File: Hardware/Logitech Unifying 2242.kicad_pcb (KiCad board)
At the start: 2 copper layers, 22 x 42 mm, 19 parts, among them J1 Bus_M.2_Socket_B, U1 TPS613222ADBV

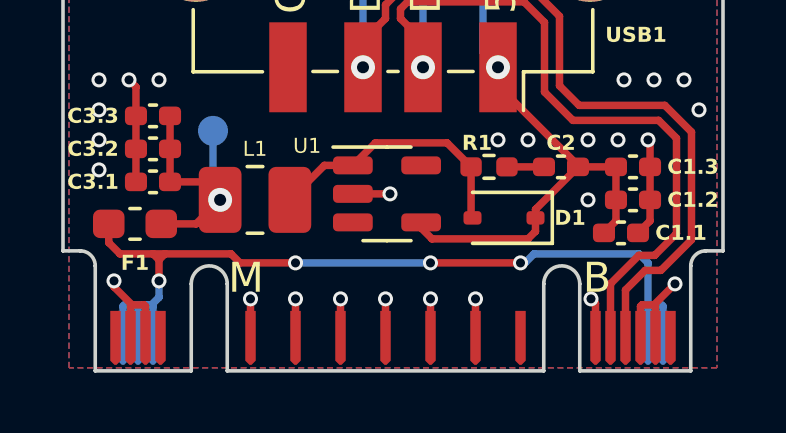
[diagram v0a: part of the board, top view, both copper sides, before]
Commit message: Adjust ground vias
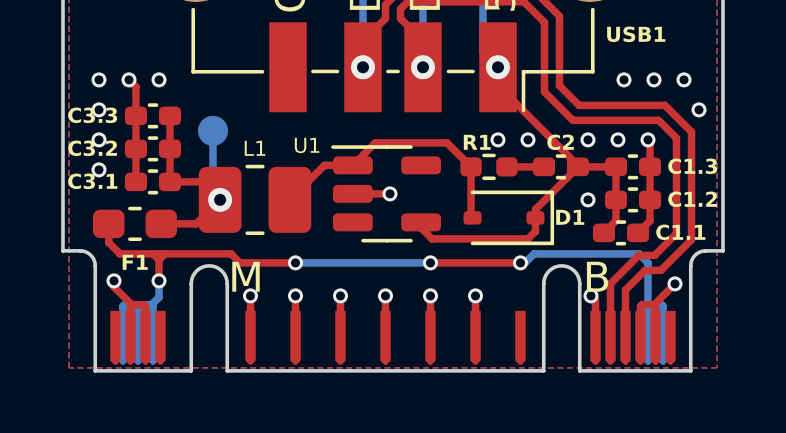
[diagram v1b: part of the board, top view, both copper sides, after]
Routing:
- net GND: track 24.5 -> 25.2 mm

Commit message: Small copper fixes
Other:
- board text added: "${TITLE} Rev.${REVISION} | ${ISSUE_DATE} ${COMMENT1}"
- board text removed: "${TITLE} Revision ${REVISION} ${COMMENT1} ${ISSUE_DATE}"
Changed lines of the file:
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@@
         (effects (font (size 1 1) (thickness 0.15)) (justify mirror))
     )
-    (fp_text user "3V3" (at 0 1.3 unlocked) (layer "B.SilkS")
+    (fp_text user "3V3" (at 0 -1.4 unlocked) (layer "B.SilkS")
         (effects (font (size 0.5 0.5) (thickness 0.1)) (justify mirror))
     )
@@
   (gr_line (start 147.1 85.2) (end 147.1 104)
     (stroke (width 0.1) (type solid)) (layer "Edge.Cuts"))
-  (gr_text "${TITLE}\nRevision ${REVISION}\n${COMMENT1}\n${ISSUE_DATE}" (at 138.6 112.8) (layer "B.SilkS")
+  (gr_text "${TITLE}\nRev.${REVISION} | ${ISSUE_DATE}\n${COMMENT1}" (at 138.6 112) (layer "B.SilkS")
     (effects (font (size 1 1) (thickness 0.2)) (justify mirror))
   )
@@
   (segment (start 132.6 113.2) (end 132.6 115.2625) (width 0.25) (layer "B.Cu") (net 14))
   (segment (start 132.6 115.2625) (end 132.8375 115.5) (width 0.25) (layer "B.Cu") (net 14))
+  (zone (net 0) (net_name "") (layer "F.Cu") (hatch edge 0.508)
+    (connect_pads (clearance 0))
+    (min_thickness 0.25) (filled_areas_thickness no)
+    (keepout (tracks allowed) (vias allowed) (pads allowed) (copperpour not_allowed) (footprints allowed))
+    (fill (thermal_gap 0.25) (thermal_bridge_width 0.25))
+    (polygon
+      (pts
+        (xy 129.7 115.3)
+        (xy 130.4 115.3)
+        (xy 130.4 116.1)
+        (xy 129.7 116.1)
+      )
+    )
+  )
   (zone (net 0) (net_name "") (layer "F.Cu") (hatch edge 0.5)
     (connect_pads (clearance 0))
@@
     (connect_pads (clearance 0.25))
     (min_thickness 0.25) (filled_areas_thickness no)
-    (fill yes (thermal_gap 0.15) (thermal_bridge_width 0.25))
+    (fill yes (thermal_gap 0.25) (thermal_bridge_width 0.25))
     (polygon
       (pts
